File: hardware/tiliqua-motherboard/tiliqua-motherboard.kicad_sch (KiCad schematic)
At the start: 27 parts, among them J2 Conn_02x06_Top_Bottom, J3 Conn_02x06_Top_Bottom, J8 MICROMOD-2222, U11 Si5351A-B-GT, U6 74AUC1G79, Y2 25MHz AMB8G

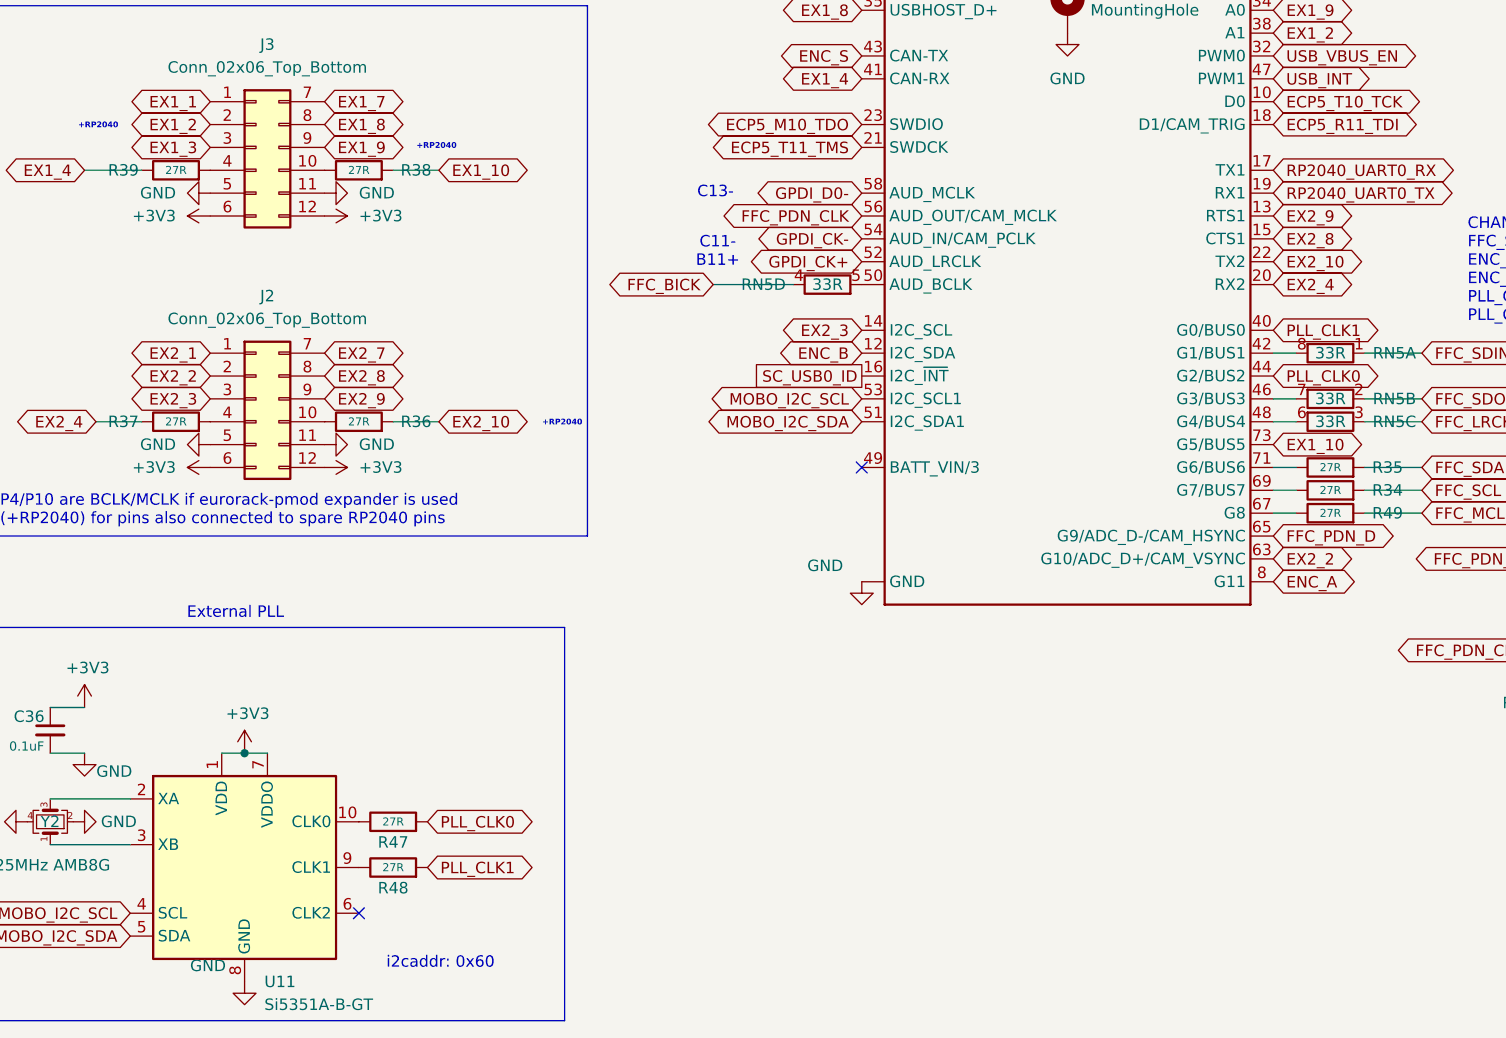
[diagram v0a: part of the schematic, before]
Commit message: * update DNP entries, add nlnet logo
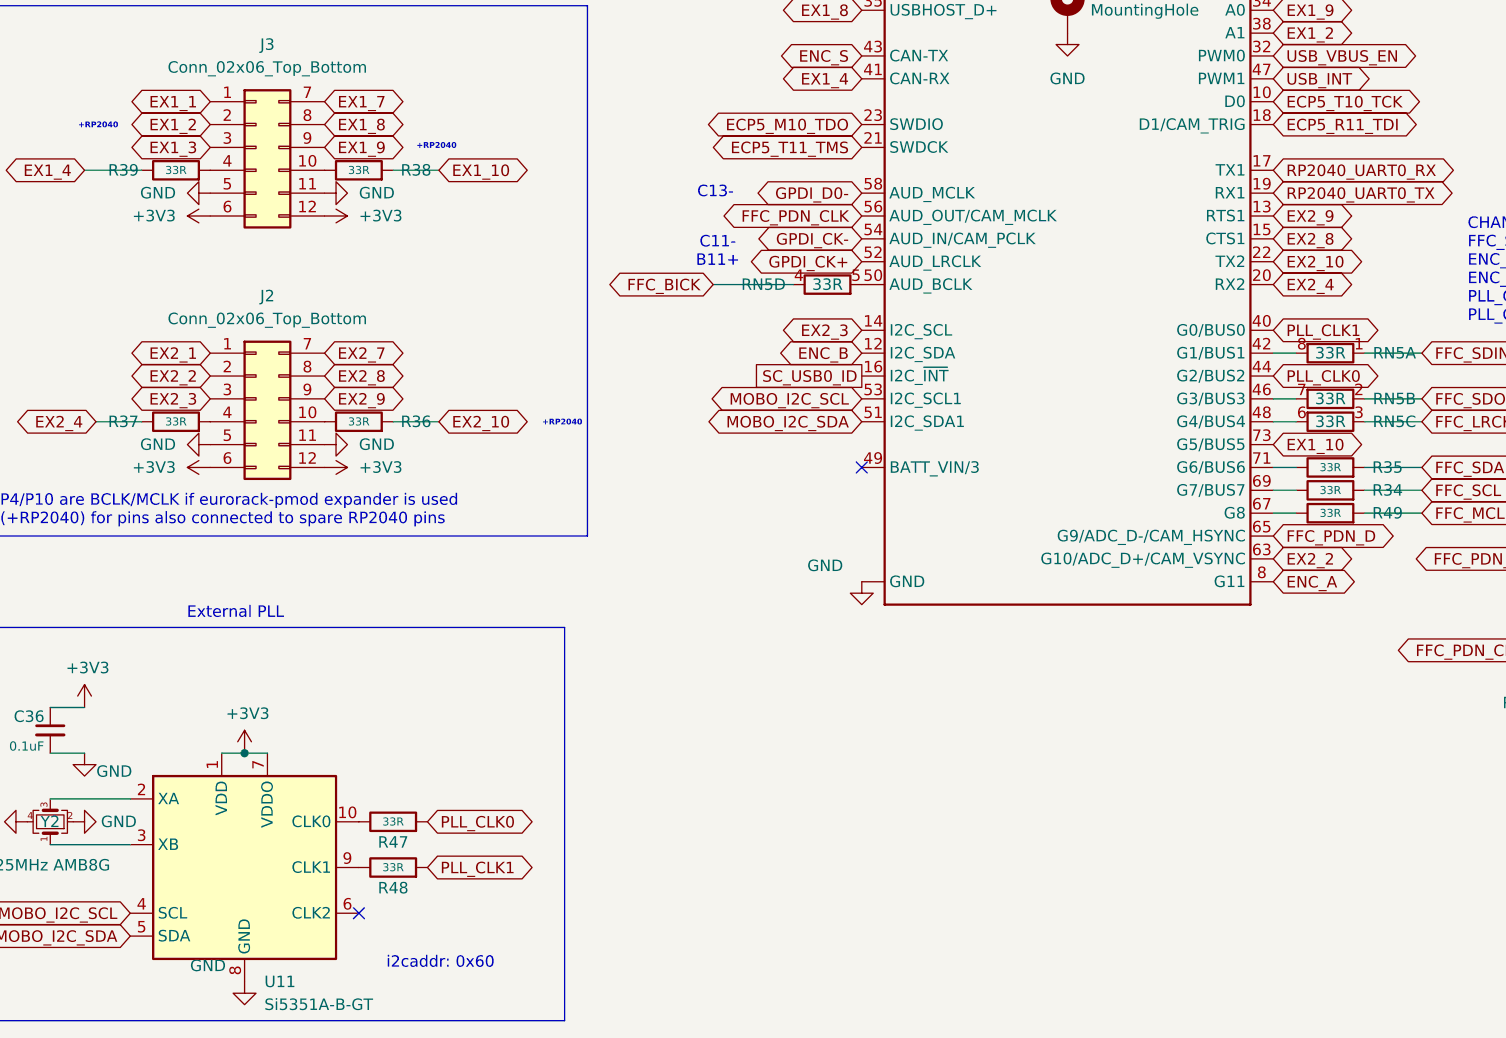
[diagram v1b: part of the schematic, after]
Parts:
- H3: now in the parts list
- R34, R35, R36, R37, R38, R39, R47, R48, R49: value 27R -> 33R; lcsc# C138021 -> C138002
- R46: now left out of the parts list
- RN5, RN8: lcsc# C125323 -> C125323
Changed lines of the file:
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@@
 			)
 		)
-		(property "Value" "27R"
+		(property "Value" "33R"
 			(at 63.5 101.6 0)
 			(effects
@@
 			)
 		)
-		(property "lcsc#" "C138021"
+		(property "lcsc#" "C138002"
 			(at 63.5 101.6 0)
 			(effects
@@
 			)
 		)
-		(property "Value" "27R"
+		(property "Value" "33R"
 			(at 171.45 137.16 0)
 			(effects
@@
 			)
 		)
-		(property "lcsc#" "C138021"
+		(property "lcsc#" "C138002"
 			(at 171.45 137.16 0)
 			(effects
@@
 			)
 		)
-		(property "lcsc#" "C125323"
+		(property "lcsc#" "C125323 "
 			(at 171.45 121.92 0)
 			(effects
@@
 			)
 		)
-		(property "Value" "27R"
+		(property "Value" "33R"
 			(at 67.31 179.07 0)
 			(effects
@@
 			)
 		)
-		(property "lcsc#" "C138021"
+		(property "lcsc#" "C138002"
 			(at 67.31 179.07 0)
 			(effects
@@
 			)
 		)
-		(property "lcsc#" "C125323"
+		(property "lcsc#" "C125323 "
 			(at 274.32 119.38 0)
 			(effects
@@
 		(unit 1)
 		(exclude_from_sim yes)
-		(in_bom no)
+		(in_bom yes)
 		(on_board yes)
 		(dnp no)
@@
 		(unit 1)
 		(exclude_from_sim no)
-		(in_bom yes)
+		(in_bom no)
 		(on_board yes)
 		(dnp yes)
@@
 			)
 		)
-		(property "lcsc#" "C125323"
+		(property "lcsc#" "C125323 "
 			(at 274.32 116.84 0)
 			(effects
@@
 			)
 		)
-		(property "Value" "27R"
+		(property "Value" "33R"
 			(at 67.31 173.99 0)
 			(effects
@@
 			)
 		)
-		(property "lcsc#" "C138021"
+		(property "lcsc#" "C138002"
 			(at 67.31 173.99 0)
 			(effects
@@
 			)
 		)
-		(property "Value" "27R"
+		(property "Value" "33R"
 			(at 171.45 139.7 0)
 			(effects
@@
 			)
 		)
-		(property "lcsc#" "C138021"
+		(property "lcsc#" "C138002"
 			(at 171.45 139.7 0)
 			(effects
@@
 			)
 		)
-		(property "lcsc#" "C125323"
+		(property "lcsc#" "C125323 "
 			(at 171.45 129.54 0)
 			(effects
@@
 			)
 		)
-		(property "lcsc#" "C125323"
+		(property "lcsc#" "C125323 "
 			(at 274.32 121.92 0)
 			(effects
@@
 			)
 		)
-		(property "Value" "27R"
+		(property "Value" "33R"
 			(at 171.45 134.62 0)
 			(effects
@@
 			)
 		)
-		(property "lcsc#" "C138021"
+		(property "lcsc#" "C138002"
 			(at 171.45 134.62 0)
 			(effects
@@
 			)
 		)
-		(property "Value" "27R"
+		(property "Value" "33R"
 			(at 43.18 129.54 0)
 			(effects
@@
 			)
 		)
-		(property "lcsc#" "C138021"
+		(property "lcsc#" "C138002"
 			(at 43.18 129.54 0)
 			(effects
@@
 			)
 		)
-		(property "Value" "27R"
+		(property "Value" "33R"
 			(at 43.18 101.6 0)
 			(effects
@@
 			)
 		)
-		(property "lcsc#" "C138021"
+		(property "lcsc#" "C138002"
 			(at 43.18 101.6 0)
 			(effects
@@
 			)
 		)
-		(property "lcsc#" "C125323"
+		(property "lcsc#" "C125323 "
 			(at 274.32 114.3 0)
 			(effects
@@
 			)
 		)
-		(property "lcsc#" "C125323"
+		(property "lcsc#" "C125323 "
 			(at 171.45 127 0)
 			(effects
@@
 			)
 		)
-		(property "Value" "27R"
+		(property "Value" "33R"
 			(at 63.5 129.54 0)
 			(effects
@@
 			)
 		)
-		(property "lcsc#" "C138021"
+		(property "lcsc#" "C138002"
 			(at 63.5 129.54 0)
 			(effects
@@
 			)
 		)
-		(property "lcsc#" "C125323"
+		(property "lcsc#" "C125323 "
 			(at 115.57 114.3 0)
 			(effects

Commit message: * fab 05.01.24
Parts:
- added R40, R41: 33R, Resistor_SMD:R_0402_1005Metric, symbol OLIMEX_RCL:R
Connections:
- net MOBO_I2C_SCL: now also R40.2
- net MOBO_I2C_SDA: now also R41.2
- new net rp2040_jtag/I2C0_SCL: R40.1
- new net rp2040_jtag/I2C0_SDA: R41.1
